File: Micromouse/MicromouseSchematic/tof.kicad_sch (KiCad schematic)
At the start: 7 parts, among them U1 VL53L1CXV0FY1

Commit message: added resistors
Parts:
- R1, R2, R3, R4: footprint (none) -> Resistor_SMD:R_0603_1608Metric
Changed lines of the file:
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@@
 			)
 		)
-		(property "Footprint" ""
+		(property "Footprint" "Resistor_SMD:R_0603_1608Metric"
 			(at 84.582 88.9 90)
 			(effects
@@
 			)
 		)
-		(property "Footprint" ""
+		(property "Footprint" "Resistor_SMD:R_0603_1608Metric"
 			(at 99.822 88.9 90)
 			(effects
@@
 			)
 		)
-		(property "Footprint" ""
+		(property "Footprint" "Resistor_SMD:R_0603_1608Metric"
 			(at 107.442 88.9 90)
 			(effects
@@
 			)
 		)
-		(property "Footprint" ""
+		(property "Footprint" "Resistor_SMD:R_0603_1608Metric"
 			(at 92.202 88.9 90)
 			(effects

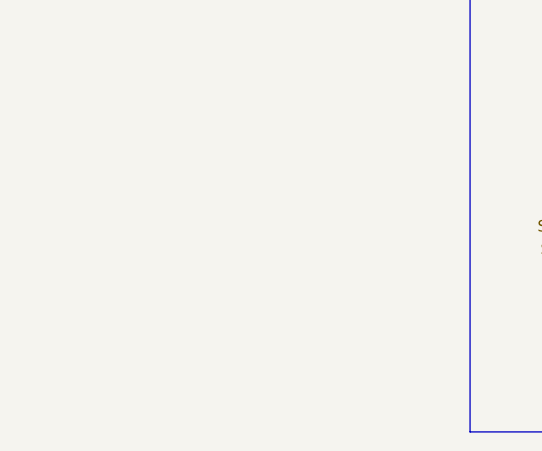
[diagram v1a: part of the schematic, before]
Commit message: Add ToF sensor connector (J13) to schematic and did TOF PCB layout
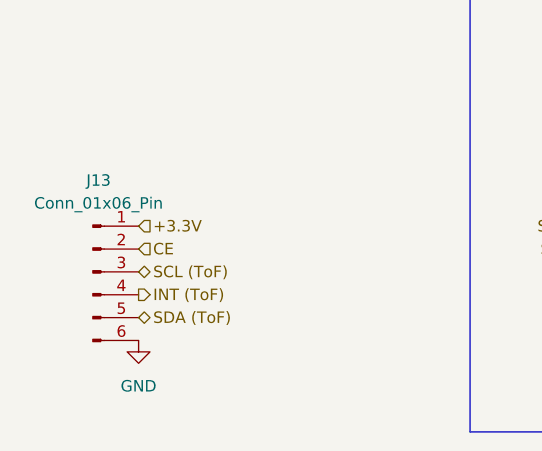
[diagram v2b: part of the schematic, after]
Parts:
- added J13: Conn_01x06_Pin, Connector_JST:JST_ZH_B6B-ZR_1x06_P1.50mm_Vertical, symbol Connector:Conn_01x06_Pin
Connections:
- net +3.3V: now also J13.1 (Pin_1)
- net CE: now also J13.2 (Pin_2)
- net GND: now also J13.6 (Pin_6)
- net INT (ToF): now also J13.4 (Pin_4)
- net SCL (ToF): now also J13.3 (Pin_3)
- net SDA (ToF): now also J13.5 (Pin_5)
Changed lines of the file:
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@@
+		)
+	)
+	(hierarchical_label "SCL (ToF)"
+		(shape bidirectional)
+		(at 26.67 104.14 0)
+		(effects
+			(font
+				(size 1.27 1.27)
+			)
+			(justify left)
 		)
 	)
@@
 		)
 	)
+	(hierarchical_label "+3.3V"
+		(shape input)
+		(at 26.67 99.06 0)
+		(effects
+			(font
+				(size 1.27 1.27)
+			)
+			(justify left)
+		)
+	)
 	(hierarchical_label "SDA (ToF)"
 		(shape bidirectional)
@@
 		)
 	)
+	(hierarchical_label "SDA (ToF)"
+		(shape bidirectional)
+		(at 26.67 109.22 0)
+		(effects
+			(font
+				(size 1.27 1.27)
+			)
+			(justify left)
+		)
+	)
 	(hierarchical_label "SCL (ToF)"
 		(shape bidirectional)
@@
 		)
 	)
+	(hierarchical_label "CE"
+		(shape input)
+		(at 26.67 101.6 0)
+		(effects
+			(font
+				(size 1.27 1.27)
+			)
+			(justify left)
+		)
+	)
 	(hierarchical_label "+3.3V"
 		(shape input)
@@
 			)
 			(justify right)
+		)
+	)
+	(hierarchical_label "INT (ToF)"
+		(shape output)
+		(at 26.67 106.68 0)
+		(effects
+			(font
+				(size 1.27 1.27)
+			)
+			(justify left)
 		)
 	)
@@
 					(unit 1)
 				)
+			)
+		)
+	)
+	(symbol
+		(lib_id "power:GND")
+		(at 26.67 111.76 0)
+		(unit 1)
+		(exclude_from_sim no)
+		(in_bom yes)
+		(on_board yes)
+		(dnp no)
+		(fields_autoplaced yes)
+		(property "Reference" "#PWR016"
+			(at 26.67 118.11 0)
+			(effects
+				(font
+					(size 1.27 1.27)
+				)
+				(hide yes)
+			)
+		)
+		(property "Value" "GND"
+			(at 26.67 116.84 0)
+			(effects
+				(font
+					(size 1.27 1.27)
+				)
+			)
+		)
+		(property "Footprint" ""
+			(at 26.67 111.76 0)
+			(effects
+				(font
+					(size 1.27 1.27)
+				)
+				(hide yes)
+			)
+		)
+		(property "Datasheet" ""
+			(at 26.67 111.76 0)
+			(effects
+				(font
+					(size 1.27 1.27)
+				)
+				(hide yes)
+			)
+		)
+		(property "Description" "Power symbol creates a global label with name \"GND\" , ground"
+			(at 26.67 111.76 0)
+			(effects
+				(font
+					(size 1.27 1.27)
+				)
+				(hide yes)
+			)
+		)
+		(pin "1"
+		)
+		(instances
+			(project "MicromouseSchematic"
+				(path "/0dcfab91-6b00-43c0-ac0b-8c301cb559e5/6bad83d6-0c2f-41d0-b5ec-d26ba0ed6048"
+					(reference "#PWR016")
+					(unit 1)
+				)
+			)
+		)
+	)
+	(symbol
+		(lib_id "Connector:Conn_01x06_Pin")
+		(at 21.59 104.14 0)
+		(unit 1)
+		(exclude_from_sim no)
+		(in_bom yes)
+		(on_board yes)
+		(dnp no)
+		(fields_autoplaced yes)
+		(property "Reference" "J13"
+			(at 22.225 93.98 0)
+			(effects
+				(font
+					(size 1.27 1.27)
+				)
+			)
+		)
+		(property "Value" "Conn_01x06_Pin"
+			(at 22.225 96.52 0)
+			(effects
+				(font
+					(size 1.27 1.27)
+				)
+			)
+		)
+		(property "Footprint" "Connector_JST:JST_ZH_B6B-ZR_1x06_P1.50mm_Vertical"
+			(at 21.59 104.14 0)
+			(effects
+				(font
+					(size 1.27 1.27)
+				)
+				(hide yes)
+			)
+		)
+		(property "Datasheet" "~"
+			(at 21.59 104.14 0)
+			(effects
+				(font
+					(size 1.27 1.27)
+				)
+				(hide yes)
+			)
+		)
+		(property "Description" "Generic connector, single row, 01x06, script generated"
+			(at 21.59 104.14 0)
+			(effects
+				(font
+					(size 1.27 1.27)
+				)
+				(hide yes)
+			)
+		)
+		(pin "1"
+		)
+		(pin "2"
+		)
+		(pin "3"
+		)
+		(pin "4"
+		)
+		(pin "5"
+		)
+		(pin "6"
+		)
+		(instances
+			(project ""
+				(path "/0dcfab91-6b00-43c0-ac0b-8c301cb559e5/6bad83d6-0c2f-41d0-b5ec-d26ba0ed6048"
+					(reference "J13")
+					(unit 1)
+				)
